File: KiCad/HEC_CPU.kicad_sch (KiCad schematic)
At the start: 19 parts, among them J3 Conn_02x05_Odd_Even, SW2 SW_Push, U1 Z80CPU, U16 74LS32, U20 74LS574, U21 74LS574, U22 74LS02, U30 74LS74, U34 74LS393, U36 74LS574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

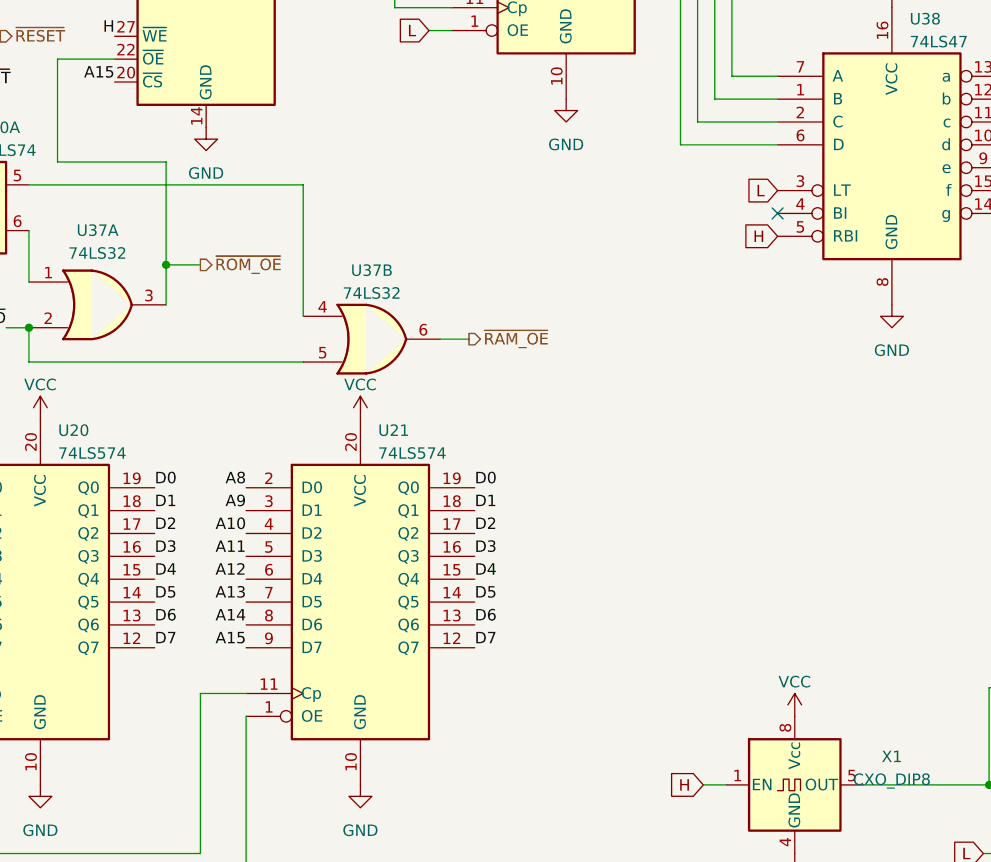
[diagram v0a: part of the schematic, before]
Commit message: Add prototyping region
Add some prototyping regions to the board, since there WILL be bugs!
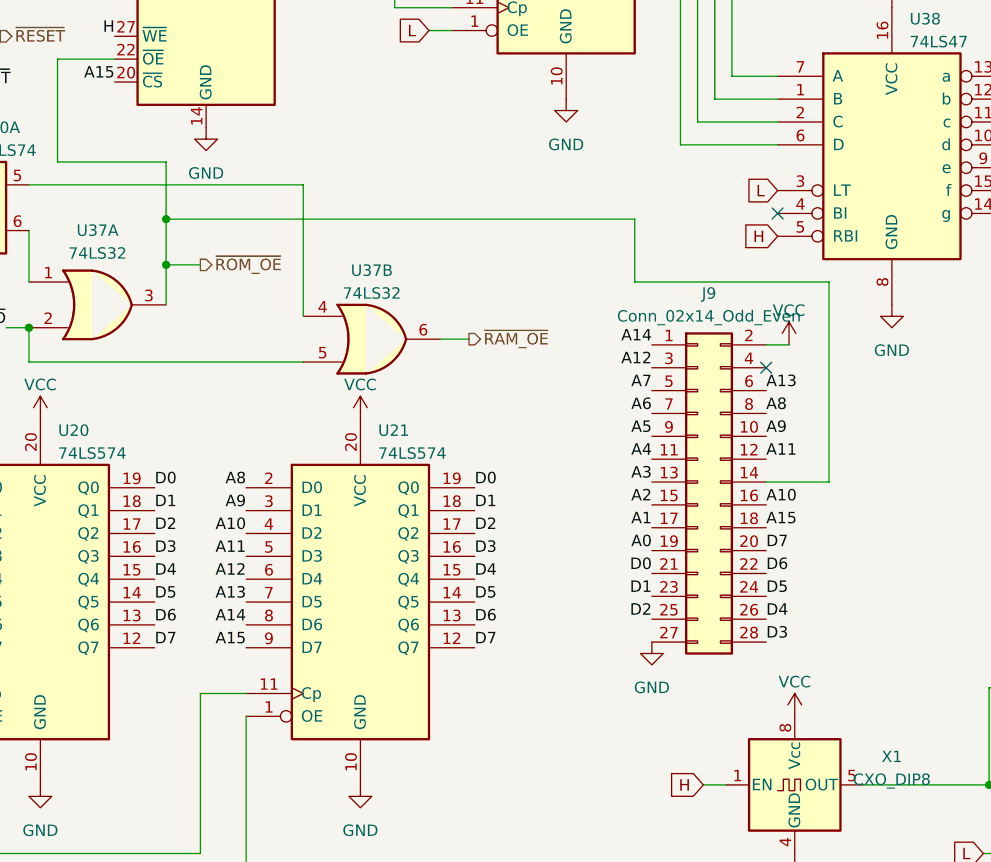
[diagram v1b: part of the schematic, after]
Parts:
- added J9: Conn_02x14_Odd_Even, Connector_PinHeader_2.54mm:PinHeader_2x14_P2.54mm_Vertical, symbol Connector_Generic:Conn_02x14_Odd_Even
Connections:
- net A0: now also J9.19 (Pin_19)
- net A1: now also J9.17 (Pin_17)
- net A10: now also J9.16 (Pin_16)
- net A11: now also J9.12 (Pin_12)
- net A12: now also J9.3 (Pin_3)
- net A13: now also J9.6 (Pin_6)
- net A14: now also J9.1 (Pin_1)
- net A15: now also J9.18 (Pin_18)
- net A2: now also J9.15 (Pin_15)
- net A3: now also J9.13 (Pin_13)
- net A4: now also J9.11 (Pin_11)
- net A5: now also J9.9 (Pin_9)
- net A6: now also J9.7 (Pin_7)
- net A7: now also J9.5 (Pin_5)
- net A8: now also J9.8 (Pin_8)
- net A9: now also J9.10 (Pin_10)
- net D0: now also J9.21 (Pin_21)
- net D1: now also J9.23 (Pin_23)
- net D2: now also J9.25 (Pin_25)
- net D3: now also J9.28 (Pin_28)
- net D4: now also J9.26 (Pin_26)
- net D5: now also J9.24 (Pin_24)
- net D6: now also J9.22 (Pin_22)
- net D7: now also J9.20 (Pin_20)
- net GND: now also J9.27 (Pin_27)
- net VCC: now also J9.2 (Pin_2)
- net ~{ROM_OE}: now also J9.14 (Pin_14)
- no-connect marks 5 -> 6

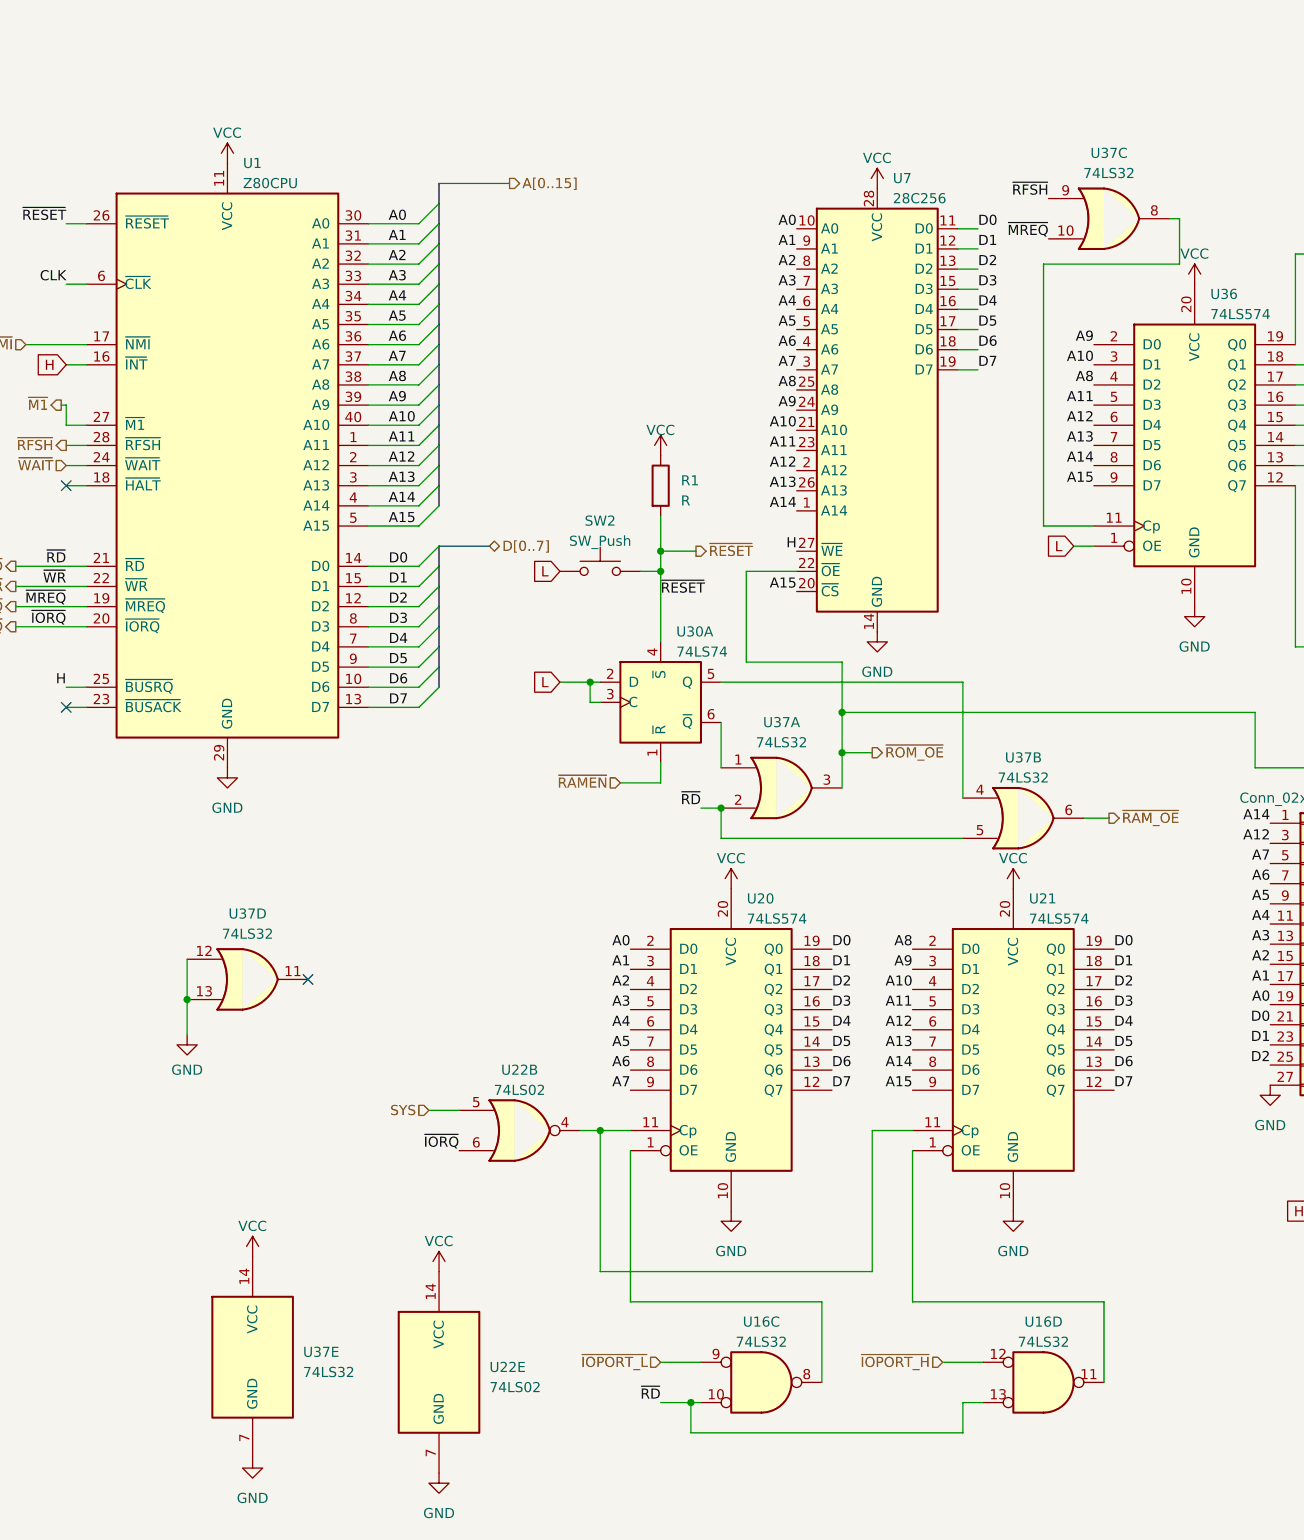
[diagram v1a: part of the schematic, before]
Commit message: More routing
Swapped U15 and U16, minor adjustments to schematic. routing of power lines.
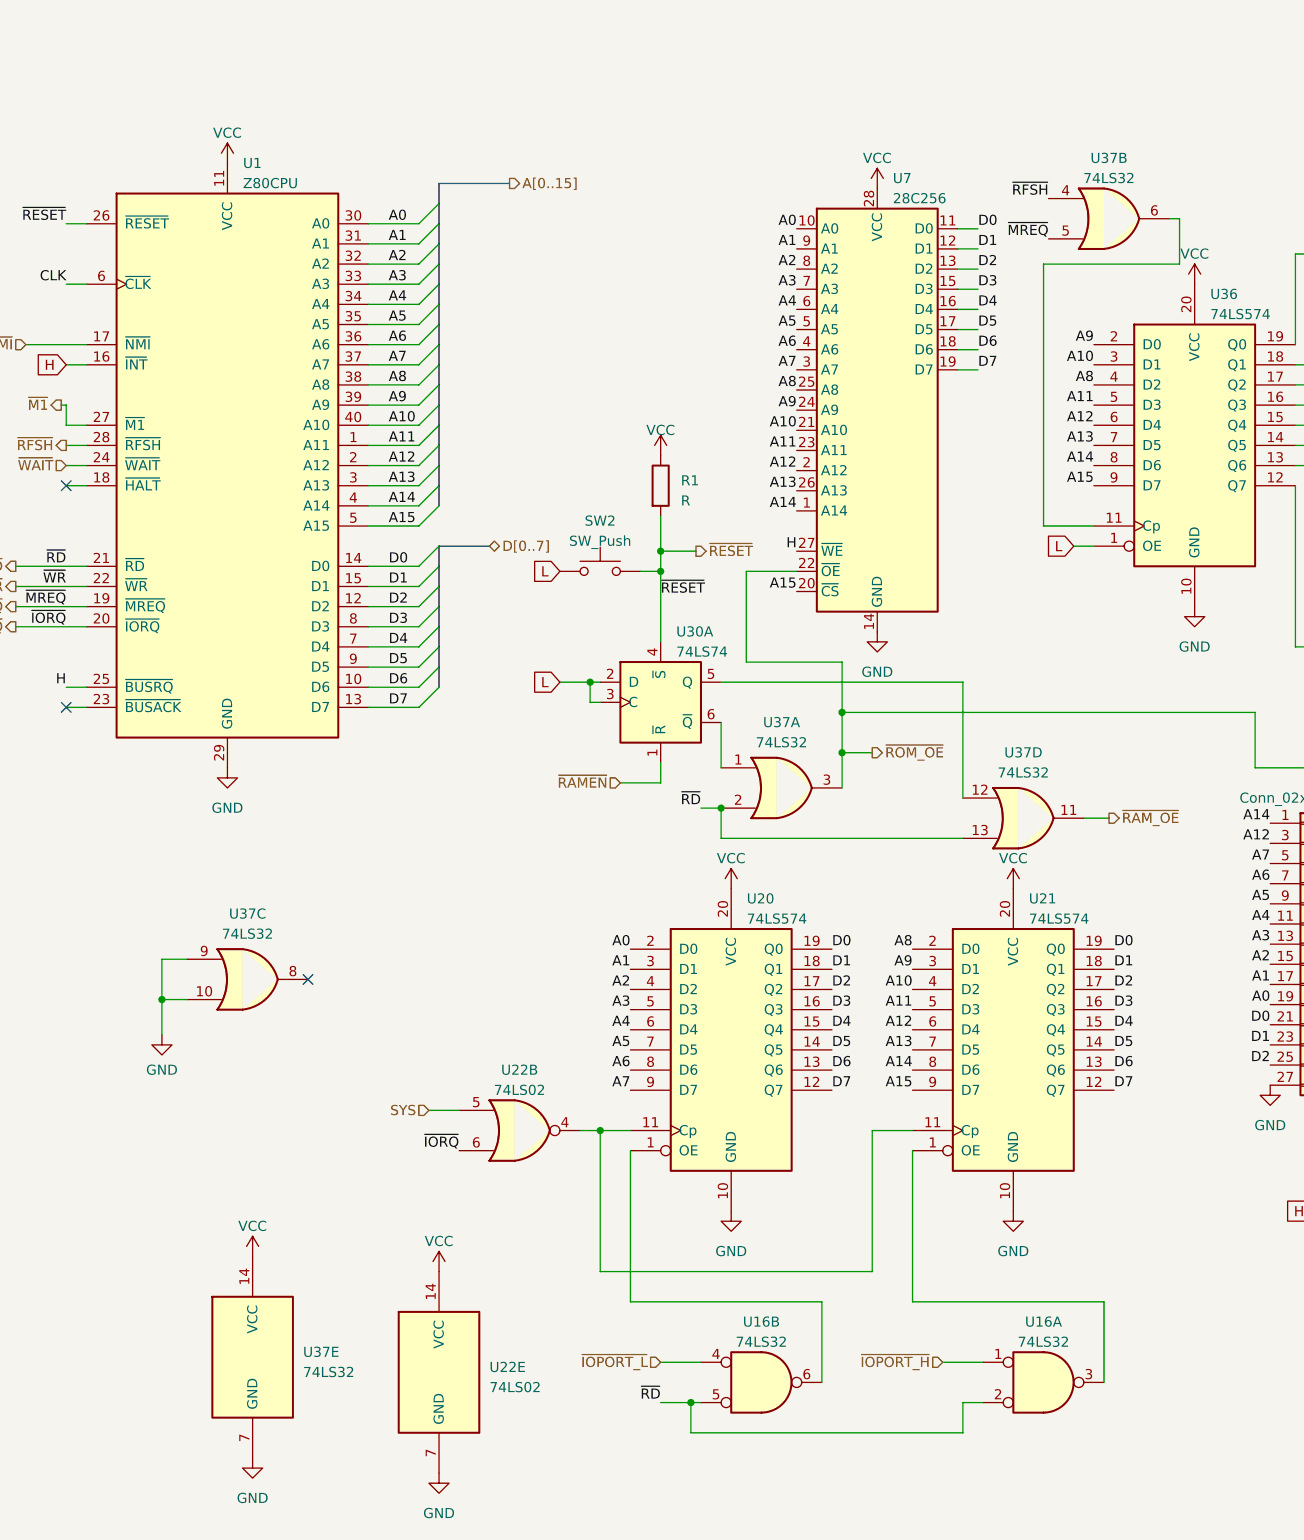
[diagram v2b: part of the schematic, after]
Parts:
- removed U16: 74LS32, Package_DIP:DIP-14_W7.62mm_Socket, symbol 74xx:74LS32
- added U16: 74LS32, Package_DIP:DIP-14_W7.62mm_Socket, symbol 74xx:74LS32
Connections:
- net GND: now also U37.10, U37.9; no longer U37.12, U37.13
- net ~{IOPORT_H}: now also U16.1
- net ~{IOPORT_L}: now also U16.4
- net ~{MREQ}: now also U37.5; no longer U37.10
- net ~{RAM_OE}: now also U37.11; no longer U37.6
- net ~{RD}: now also U37.13, U16.2, U16.5; no longer U37.5
- net ~{RFSH}: now also U37.4; no longer U37.9
- net at U21.1 (OE): now also U16.3
- net at U20.1 (OE): now also U16.6
- net at U36.11 (Cp): now also U37.6; no longer U37.8
- net at U30.5 (Q): now also U37.12; no longer U37.4
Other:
- moved on the sheet: U37B, U37C, U37D
